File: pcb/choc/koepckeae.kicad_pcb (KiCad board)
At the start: 2 copper layers, 239.8 x 115.1 mm, 50 parts, among them J1 Conn_01x09_Socket, J2 Conn_01x02_Socket, J3 Conn_01x02_Socket, J4 Conn_01x12_Socket, K1 PG1350, K10 PG1350, K11 PG1350, K12 PG1350, K13 PG1350, K14 PG1350, K15 PG1350, K16 PG1350, K17 PG1350, K18 PG1350, K19 PG1350, K2 PG1350, K20 PG1350, K21 PG1350, K22 PG1350, K23 PG1350, K24 PG1350, K25 PG1350, K26 PG1350, K27 PG1350, K28 PG1350, K29 PG1350, K3 PG1350, K30 PG1350, K31 PG1350, K32 PG1350, K33 PG1350, K34 PG1350, K4 PG1350, K5 PG1350, K6 PG1350, K7 PG1350, K8 PG1350, K9 PG1350, SW1 SW_Push, SW2 SW_SPDT, U1 Seeeduino Xiao nRF52840, U2 74HC595

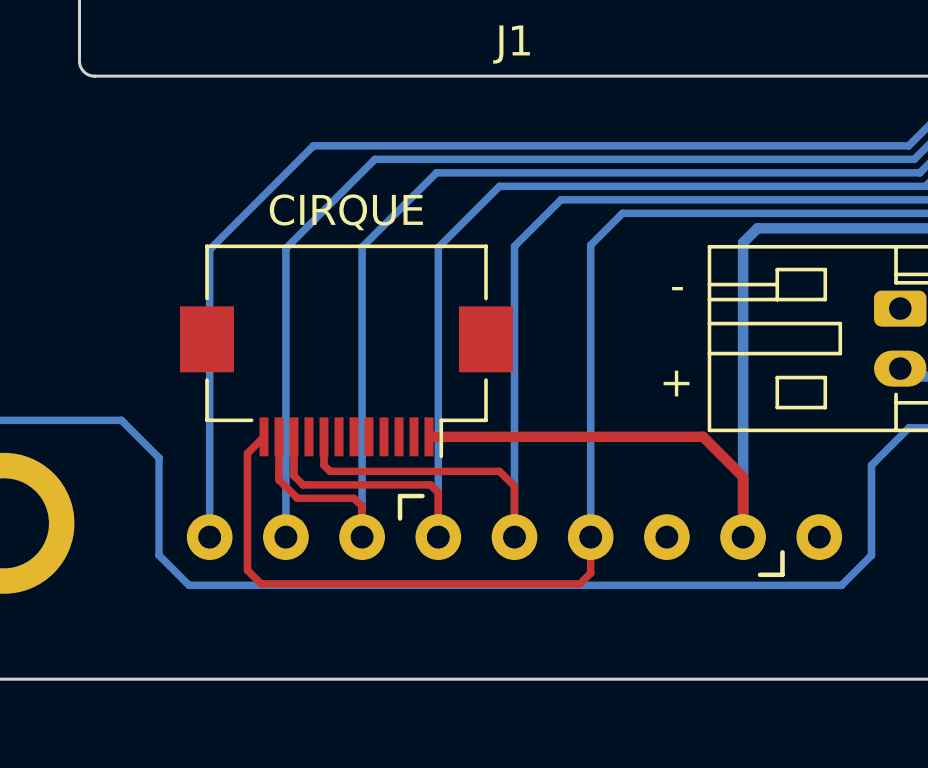
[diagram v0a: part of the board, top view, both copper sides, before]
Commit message: Remove unused fpc
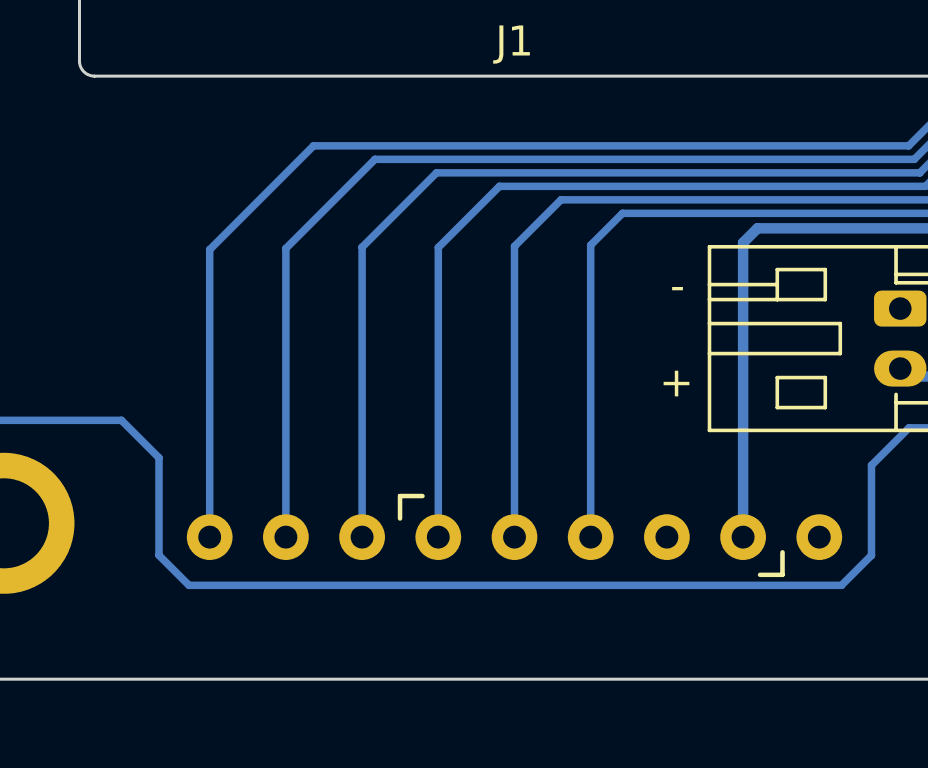
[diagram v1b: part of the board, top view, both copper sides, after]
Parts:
- removed J4: Conn_01x12_Socket, Connector_FFC-FPC:Hirose_FH12-12S-0.5SH_1x12-1MP_P0.50mm_Horizontal
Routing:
- net SCK: track 118.1 -> 100.5 mm
- net VCC: track 133.7 -> 120.7 mm
- net MOSI: track 123.9 -> 114.6 mm
- net HEADER_CS: track 112.9 -> 105.1 mm
- net MISO: track 100.3 -> 94.7 mm

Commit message: Add bottom plate gerbers
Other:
- board text added: "Display"
- board text added: "koepckeae by ssbb"
